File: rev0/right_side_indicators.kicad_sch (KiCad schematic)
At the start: 26 parts, among them IC1 ECP5-BGA256, U14 74AUP2G126, U2 74AUP2G126

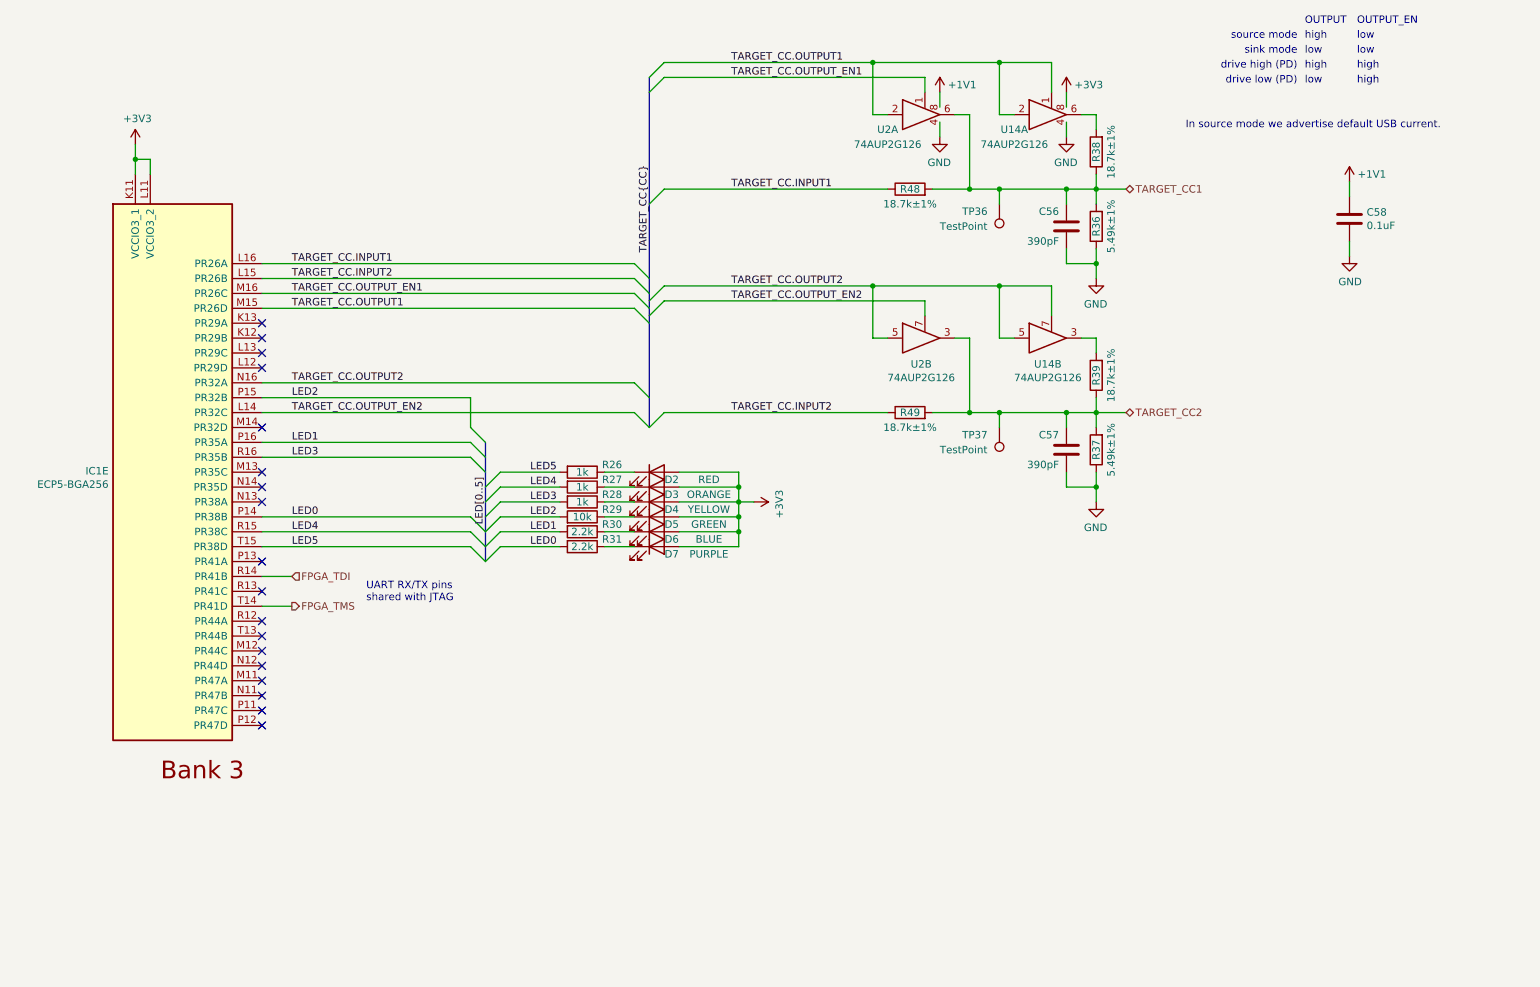
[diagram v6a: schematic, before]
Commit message: hardware: reassign FPGA I/O banks
assign HyperRAM to DQS group
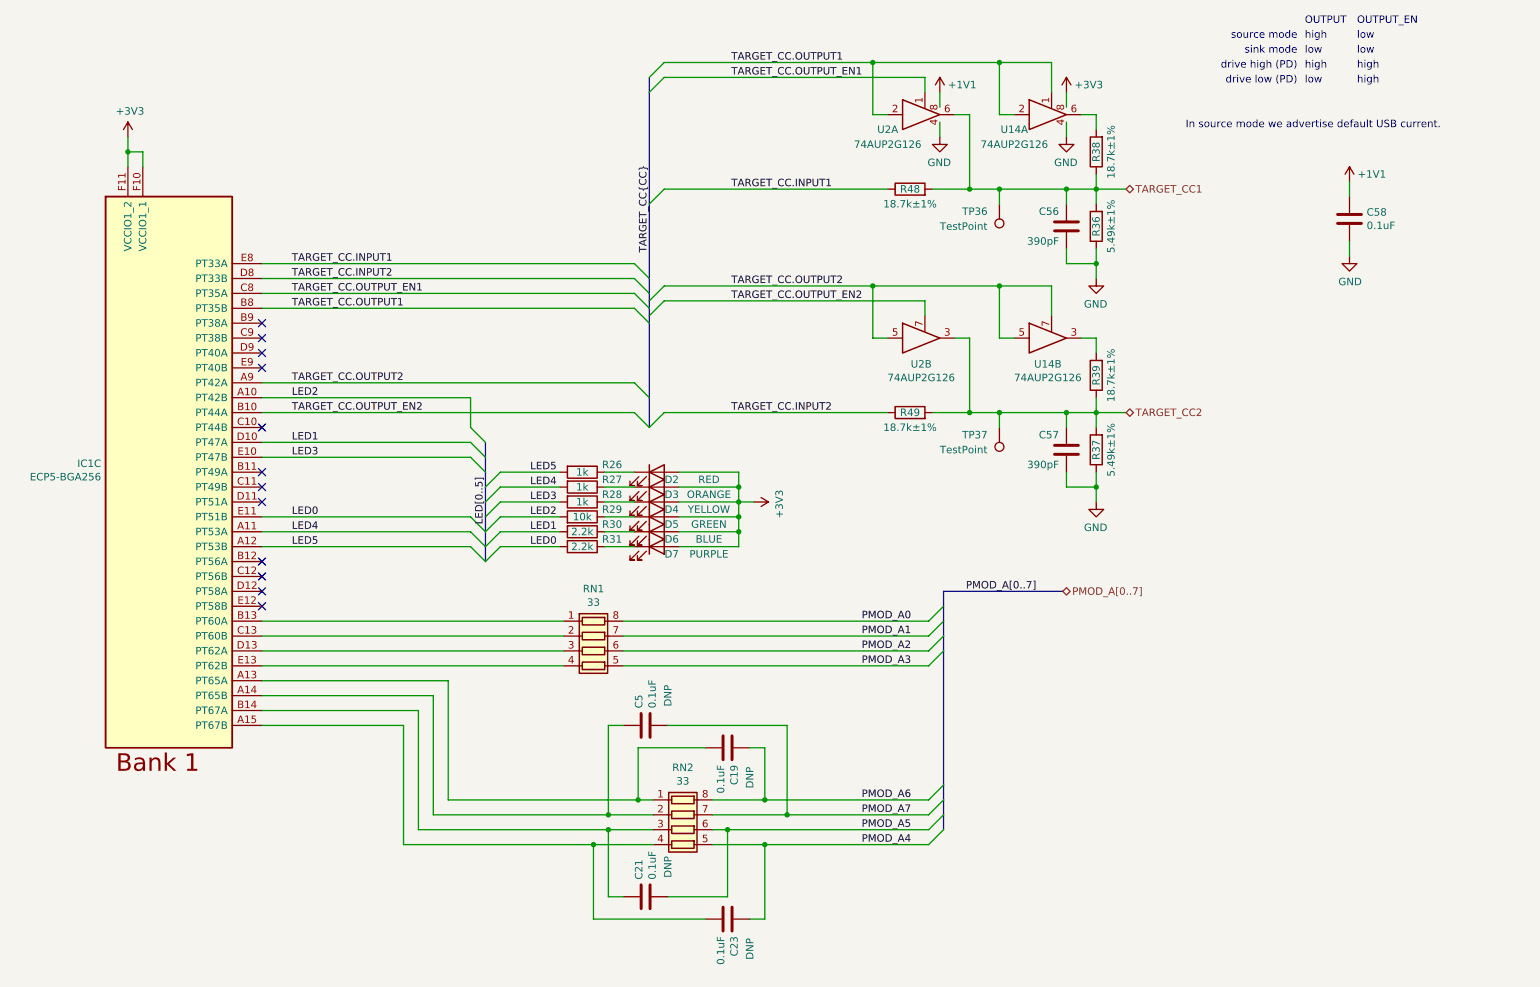
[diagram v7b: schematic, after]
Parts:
- removed IC1: ECP5-BGA256, luna:lattice_cabga256, symbol fpgas_and_processors:ECP5-BGA256
- added C19, C21, C23, C5: 0.1uF, Capacitor_SMD:C_0402_1005Metric, symbol Device:C
- added IC1: ECP5-BGA256, luna:lattice_cabga256, symbol fpgas_and_processors:ECP5-BGA256
- added RN1, RN2: 33, Resistor_SMD:R_Array_Convex_4x0402, symbol Device:R_Pack04
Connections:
- net +3V3: now also IC1.F10 (VCCIO1_1), IC1.F11 (VCCIO1_2)
- net LED0: now also IC1.E11 (PT51B)
- net LED1: now also IC1.D10 (PT47A)
- net LED2: now also IC1.A10 (PT42B)
- net LED3: now also IC1.E10 (PT47B)
- net LED4: now also IC1.A11 (PT53A)
- net LED5: now also IC1.A12 (PT53B)
- net TARGET_CC.INPUT1: now also IC1.E8 (PT33A)
- net TARGET_CC.INPUT2: now also IC1.D8 (PT33B)
- net TARGET_CC.OUTPUT1: now also IC1.B8 (PT35B)
- net TARGET_CC.OUTPUT2: now also IC1.A9 (PT42A)
- net TARGET_CC.OUTPUT_EN1: now also IC1.C8 (PT35A)
- net TARGET_CC.OUTPUT_EN2: now also IC1.B10 (PT44A)
- new net: C19.2, IC1.A13 (PT65A), RN2.1 (R1.1)
- new net: C5.1, IC1.A14 (PT65B), RN2.2 (R2.1)
- new net: C23.2, IC1.A15 (PT67B), RN2.4 (R4.1)
- new net: IC1.B13 (PT60A), RN1.1 (R1.1)
- new net: C21.1, IC1.B14 (PT67A), RN2.3 (R3.1)
- new net: IC1.C13 (PT60B), RN1.2 (R2.1)
- new net: IC1.D13 (PT62A), RN1.3 (R3.1)
- new net: IC1.E13 (PT62B), RN1.4 (R4.1)
- new net PMOD_A0: RN1.8 (R1.2)
- new net PMOD_A1: RN1.7 (R2.2)
- new net PMOD_A2: RN1.6 (R3.2)
- new net PMOD_A3: RN1.5 (R4.2)
- new net PMOD_A4: C23.1, RN2.5 (R4.2)
- new net PMOD_A5: C21.2, RN2.6 (R3.2)
- new net PMOD_A6: C19.1, RN2.8 (R1.2)
- new net PMOD_A7: C5.2, RN2.7 (R2.2)
- no-connect marks 18 -> 12
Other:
- note removed: "UART RX/TX pins shared with JTAG"
